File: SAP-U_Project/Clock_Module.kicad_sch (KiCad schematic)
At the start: 0 parts

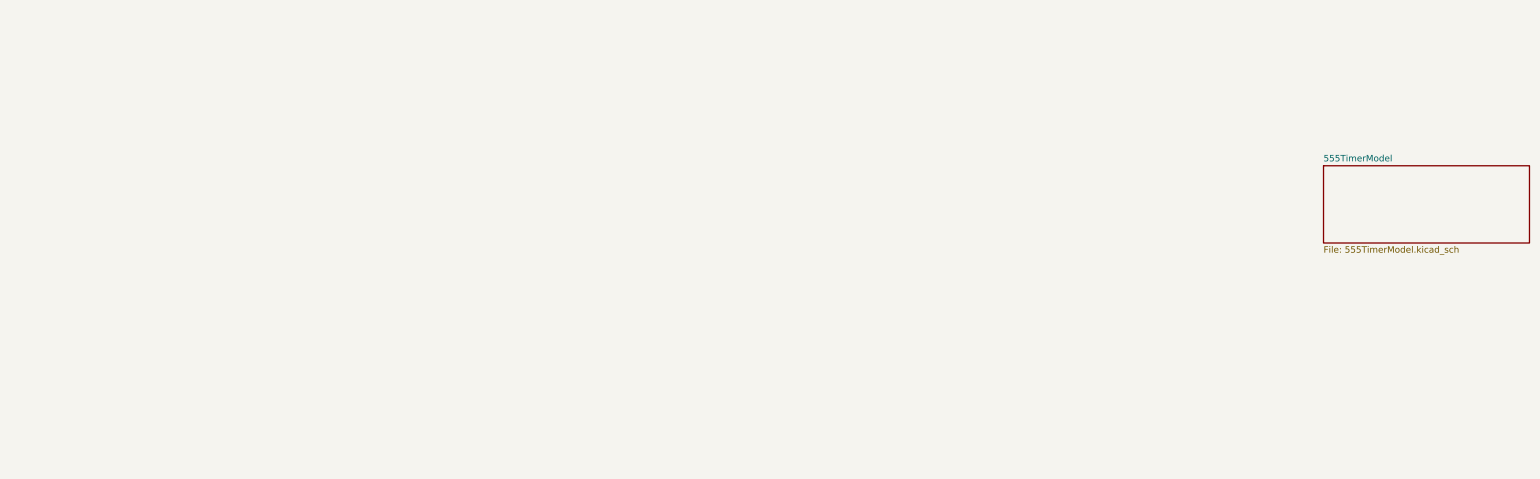
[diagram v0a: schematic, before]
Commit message: Checkpoint: created documentation and schematic for the astable portion of the clock module
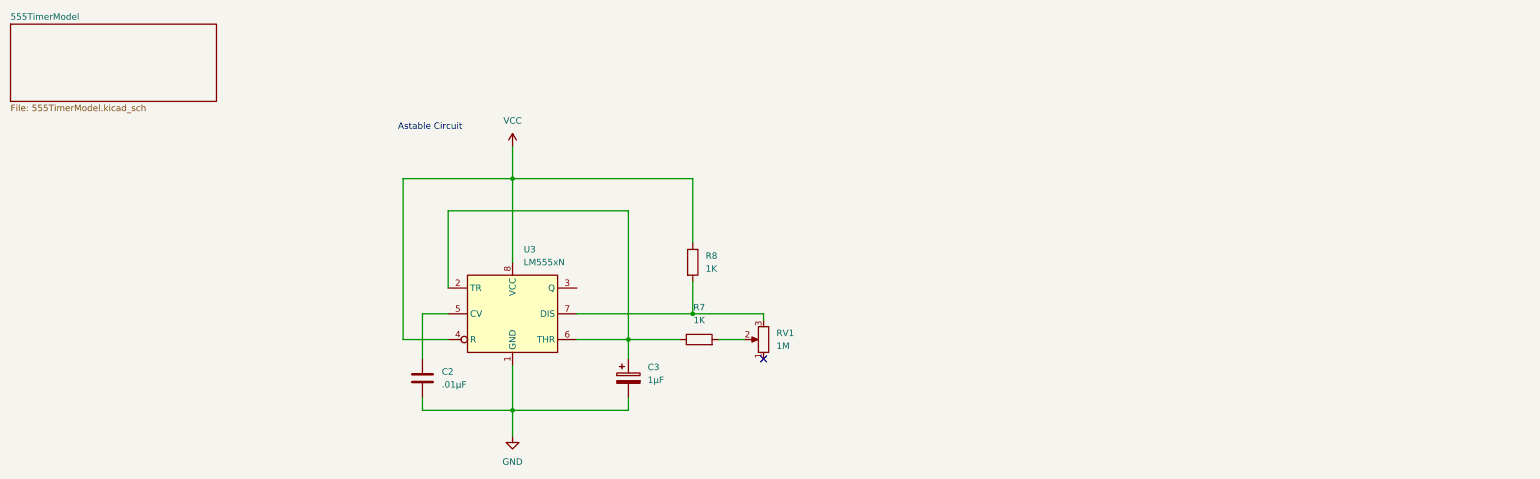
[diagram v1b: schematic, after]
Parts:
- added C2: .01µF, symbol Device:C
- added C3: 1µF, symbol Device:C_Polarized
- added R7, R8: 1K, symbol Device:R
- added RV1: 1M, symbol Device:R_Potentiometer
- added U3: LM555xN, Package_DIP:DIP-8_W7.62mm, symbol Timer:LM555xN
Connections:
- new net: R8.2, RV1.3, U3.7 (DIS)
- new net: C3.1, R7.1, U3.2 (TR), U3.6 (THR)
- new net: R7.2, RV1.2
- new net: C2.2, U3.5 (CV)
- new net GND: C2.1, C3.2, U3.1 (GND)
- new net VCC: R8.1, U3.4 (R), U3.8 (VCC)
- no-connect marks 0 -> 1
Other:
- note added: "Astable Circuit"

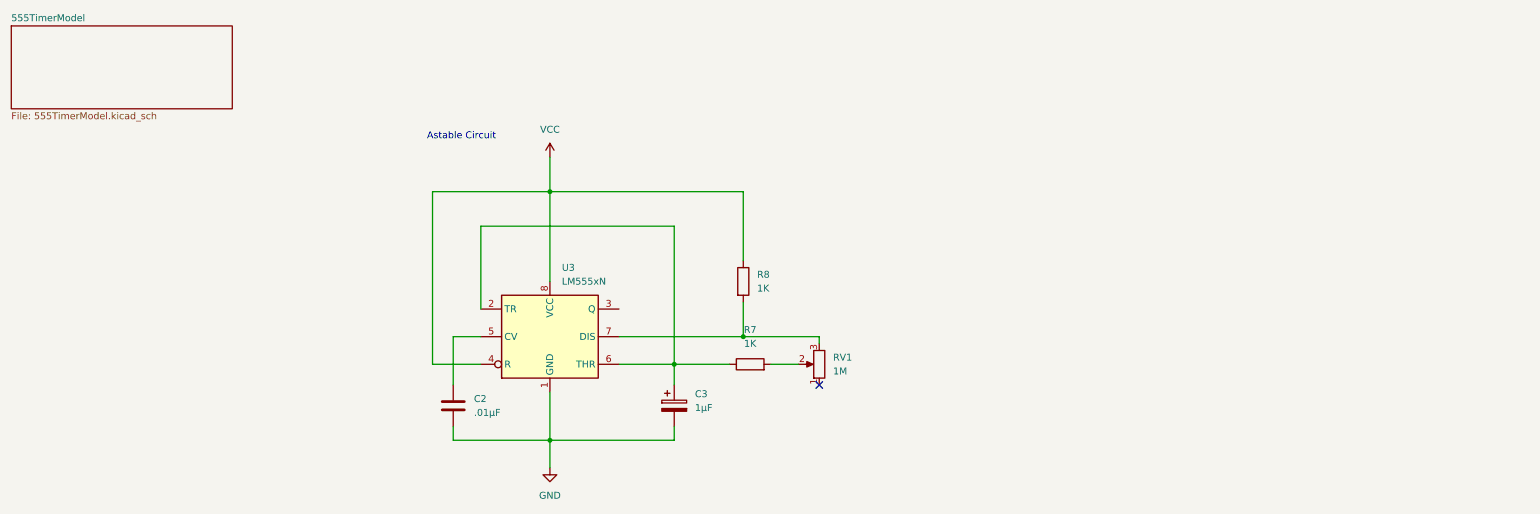
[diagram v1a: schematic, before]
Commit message: added circuit for monostable clock
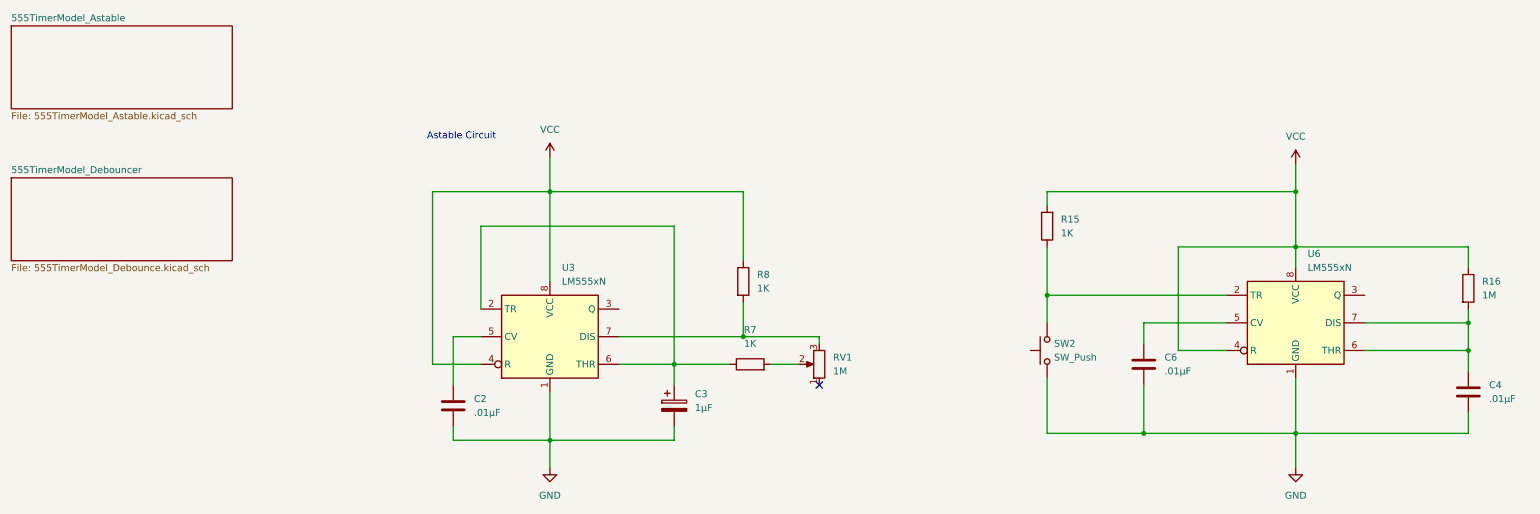
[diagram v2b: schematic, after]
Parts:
- added C4, C6: .01µF, symbol Device:C
- added R15: 1K, symbol Device:R
- added R16: 1M, symbol Device:R
- added SW2: SW_Push, symbol Switch:SW_Push
- added U6: LM555xN, Package_DIP:DIP-8_W7.62mm, symbol Timer:LM555xN
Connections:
- net GND: now also C4.1, C6.1, SW2.1, U6.1 (GND)
- net VCC: now also R15.2, R16.1, U6.4 (R), U6.8 (VCC)
- new net: R15.1, SW2.2, U6.2 (TR)
- new net: C6.2, U6.5 (CV)
- new net: C4.2, R16.2, U6.6 (THR), U6.7 (DIS)
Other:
- sheet 555TimerModel renamed 555TimerModel_Astable
- added sheet 555TimerModel_Debouncer (555TimerModel_Debounce.kicad_sch)
- sheet 555TimerModel_Astable: file 555TimerModel.kicad_sch -> 555TimerModel_Astable.kicad_sch

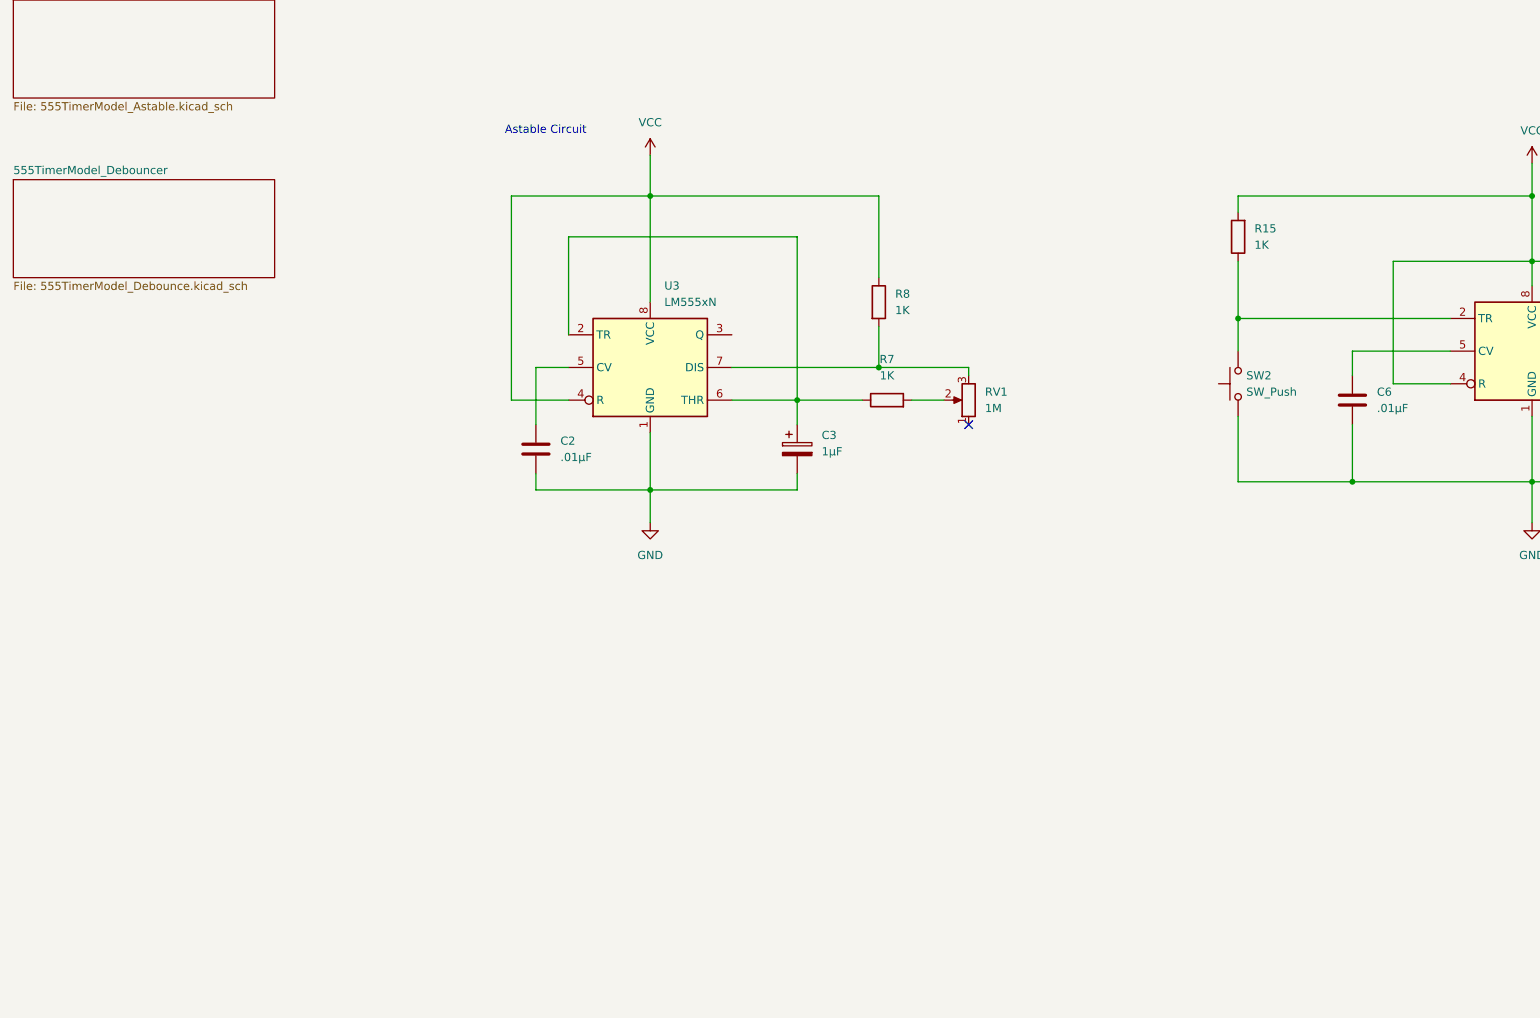
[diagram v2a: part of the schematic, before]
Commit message: Checkpoint: added circuit for Bistable
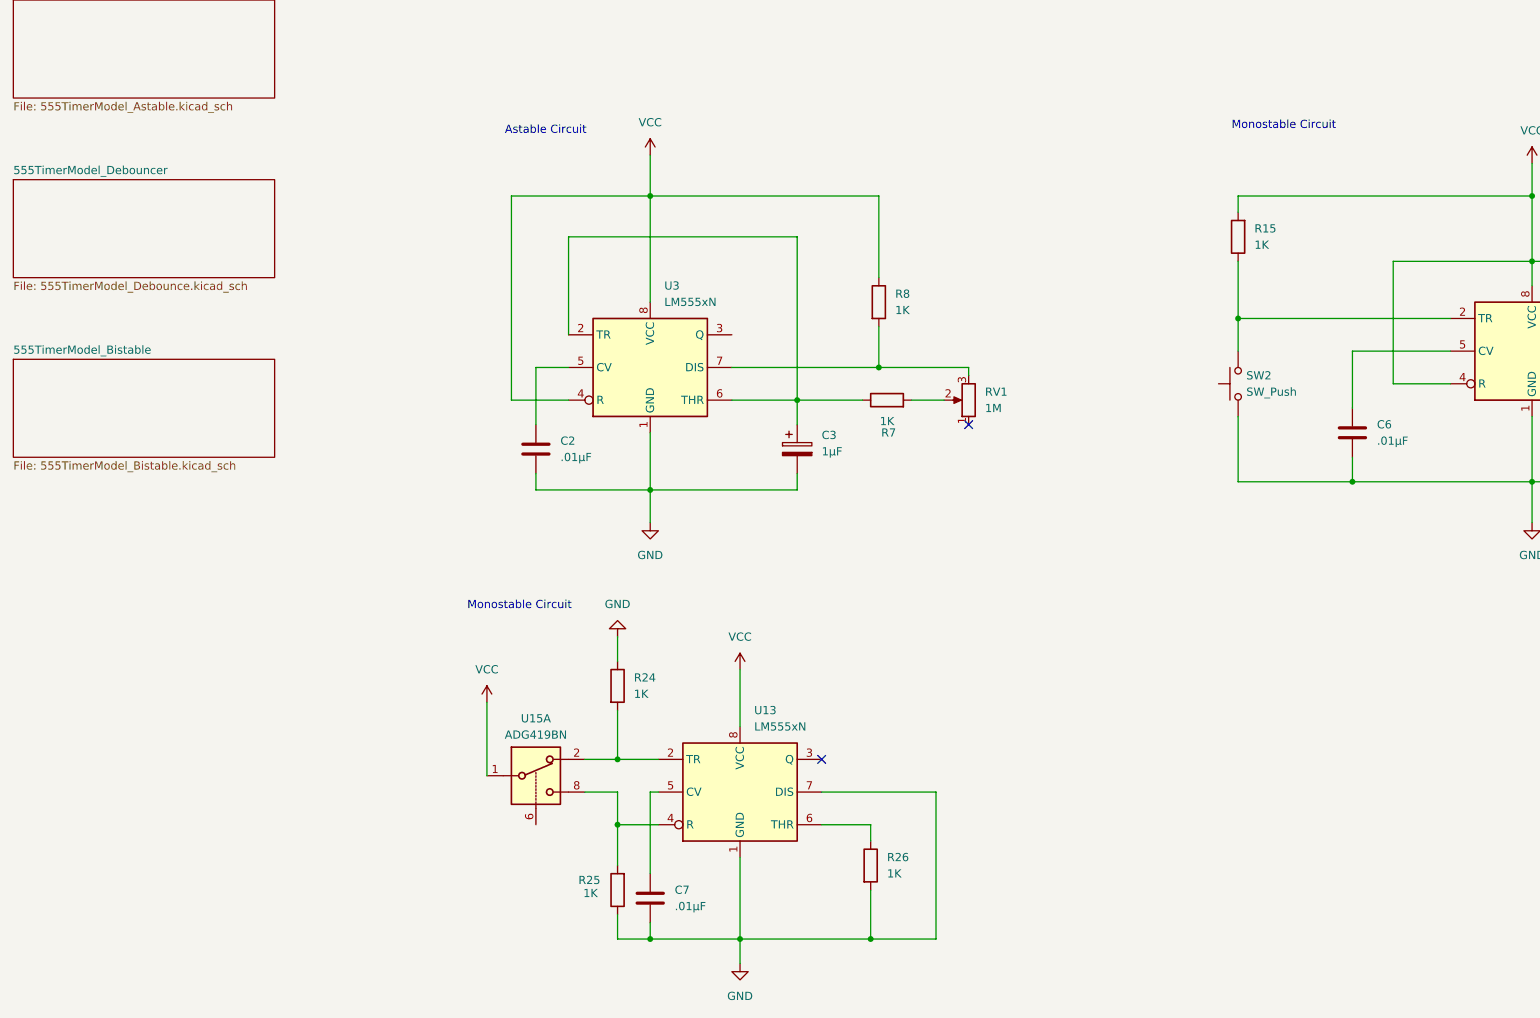
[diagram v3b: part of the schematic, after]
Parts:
- added C7: .01µF, symbol Device:C
- added R24, R25, R26: 1K, symbol Device:R
- added U13: LM555xN, Package_DIP:DIP-8_W7.62mm, symbol Timer:LM555xN
- added U15: ADG419BN, Package_DIP:DIP-8_W7.62mm, symbol Analog_Switch:ADG419BN
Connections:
- net GND: now also C7.1, R24.1, R25.1, R26.2, U13.1 (GND), U13.7 (DIS)
- net VCC: now also U13.8 (VCC), U15.1
- new net: R24.2, U13.2 (TR), U15.2
- new net: R25.2, U13.4 (R), U15.8
- new net: C7.2, U13.5 (CV)
- new net: R26.1, U13.6 (THR)
- no-connect marks 1 -> 2
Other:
- added sheet 555TimerModel_Bistable (555TimerModel_Bistable.kicad_sch)
- note added: "Monostable Circuit"
- moved on the sheet: C6
